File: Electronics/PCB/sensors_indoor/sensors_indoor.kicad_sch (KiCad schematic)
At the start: 10 parts, among them J1 B5B-ZR, U1 SHT45-AD1F, U2 LPS22DF, U3 SCD41-D-R2, U4 TSOP38436, U5 STM32WBA5MMG, U6 SGP41, U7 SPS30

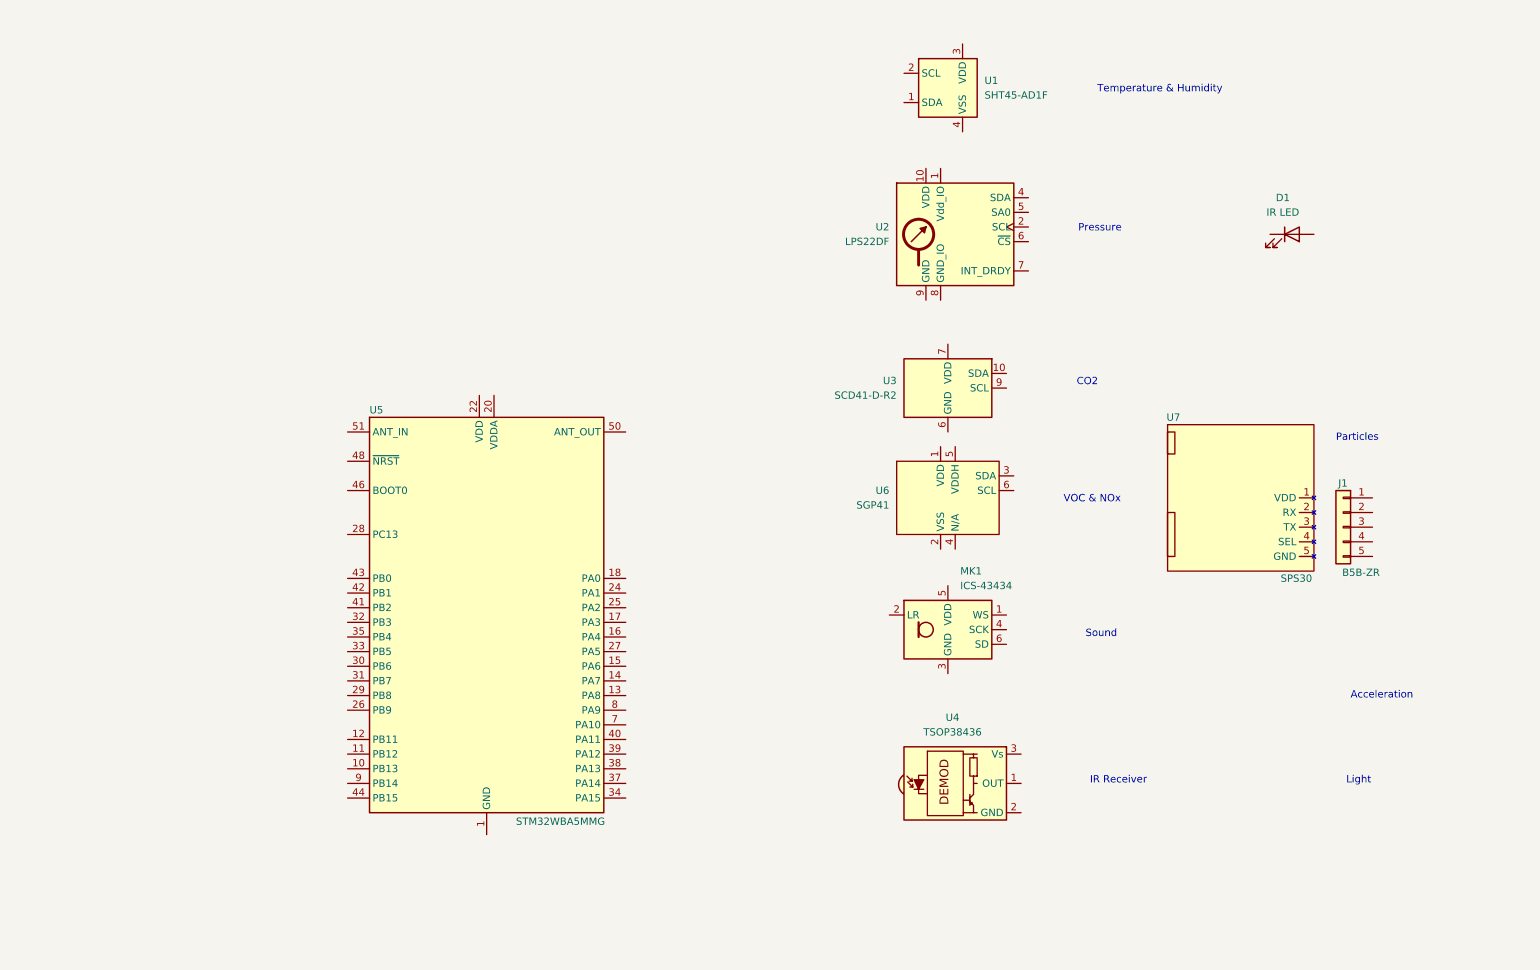
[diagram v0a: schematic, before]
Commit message: Arranged sensors on PCB, added MRAM and USB-C socket
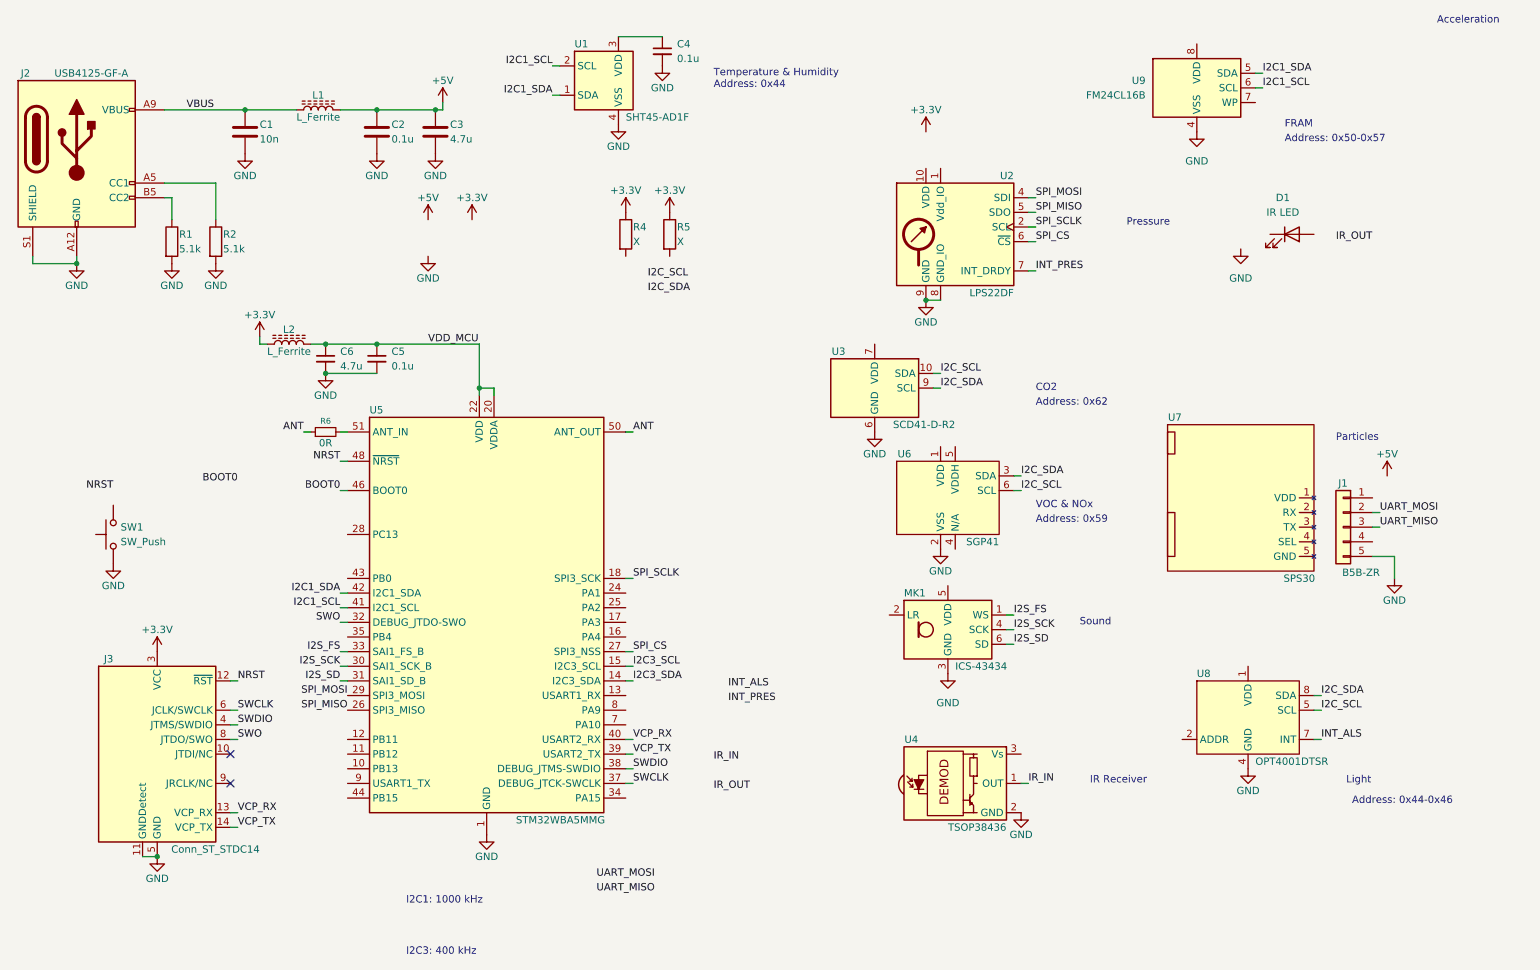
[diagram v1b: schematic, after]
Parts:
- added C1: 10n, symbol Device:C
- added C2: 0.1u, symbol Device:C
- added C3: 4.7u, symbol Device:C
- added C4, C5: 0.1u, symbol Device:C_Small
- added C6: 4.7u, symbol Device:C_Small
- added J2: USB4125-GF-A, Connector_USB:USB_C_Receptacle_GCT_USB4125-xx-x-0190_6P_TopMnt_Horizontal, symbol Connector:USB_C_Receptacle_PowerOnly_6P
- added J3: Conn_ST_STDC14, Connector_PinHeader_1.27mm:PinHeader_2x07_P1.27mm_Vertical, symbol Connector:Conn_ST_STDC14
- added L1, L2: L_Ferrite, symbol Device:L_Ferrite
- added R1, R2: 5.1k, symbol Device:R
- added R4, R5: X, symbol Device:R
- added R6: 0R, Resistor_SMD:R_0402_1005Metric, symbol Device:R_Small
- added SW1: SW_Push, symbol Switch:SW_Push
- added U8: OPT4001DTSR, DWlib:TI_SOT-5X3_OPT4001DTSR, symbol DWlib:OPT4001DTSR
- added U9: FM24CL16B, Package_SO:SOIC-8_3.9x4.9mm_P1.27mm, symbol Memory_NVRAM:FM24CL16B
- D1: footprint LED_SMD:LED_0603_1608Metric -> LED_THT:LED_D5.0mm_Clear
- U5: MPN (none) -> STM32WBA5MMGH6TR
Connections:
- net GND: now also J1.5 (Pin_5), MK1.3 (GND), U1.4 (VSS), U2.3 (GND), U2.8 (GND_IO), U2.9 (GND), U3.20 (GND), U3.21 (GND), U3.6 (GND), U4.2 (GND), U6.2 (VSS), C1.2, C2.2, C3.2, C4.2, C5.2, C6.2, J2.A12 (GND), J2.B12 (GND), J2.S1 (SHIELD), J3.11 (GNDDetect), J3.5 (GND), J3.7 (GND), R1.2, R2.2, SW1.1, U8.4 (GND), U9.4 (VSS)
- net I2C_SCL: now reaches U3.10 (SDA)
- net I2C_SCL: now also U6.6 (SCL), U8.5 (SCL)
- net I2C_SDA: now reaches U3.9 (SCL)
- net I2C_SDA: now also U6.3 (SDA), U8.8 (SDA)
- net I2S_FS: now reaches MK1.1 (WS)
- net I2S_FS: now also U5.33 (PB5)
- net I2S_SCK: now reaches MK1.4 (SCK)
- net I2S_SCK: now also U5.30 (PB6)
- net I2S_SD: now reaches MK1.6 (SD)
- net I2S_SD: now also U5.31 (PB7)
- net SPI_SCLK: now reaches U2.2 (SCL)
- net SPI_SCLK: now also U5.18 (PA0)
- net SPI_MOSI: now reaches U2.4 (SDA)
- net SPI_MOSI: now also U5.29 (PB8)
- net SPI_MISO: now reaches U2.5 (SA0)
- net SPI_MISO: now also U5.26 (PB9)
- net SPI_CS: now reaches U2.6 (~{CS})
- net SPI_CS: now also U5.27 (PA5)
- net INT_PRES: now reaches U2.7 (INT_DRDY)
- net I2C1_SDA: now reaches U1.1 (SDA)
- net I2C1_SDA: now also U5.42 (PB1), U9.5 (SDA)
- net I2C1_SCL: now reaches U1.2 (SCL)
- net I2C1_SCL: now also U5.41 (PB2), U9.6 (SCL)
- net at U1.3 (VDD): now also C4.1
- net IR_IN: now reaches U4.1 (OUT)
- net UART_MOSI: now reaches J1.2 (Pin_2)
- net UART_MISO: now reaches J1.3 (Pin_3)
- net I2C3_SDA: now reaches U5.14 (PA7)
- net I2C3_SCL: now reaches U5.15 (PA6)
- net VDD_MCU: now reaches U5.20 (VDDA)
- net VDD_MCU: now also U5.22 (VDD), C5.1, C6.1, L2.2
- net SWO: now reaches U5.32 (PB3)
- net SWO: now also J3.8 (JTDO/SWO)
- net SWCLK: now reaches U5.37 (PA14)
- net SWCLK: now also J3.6 (JCLK/SWCLK)
- net SWDIO: now reaches U5.38 (PA13)
- net SWDIO: now also J3.4 (JTMS/SWDIO)
- net VCP_TX: now reaches U5.39 (PA12)
- net VCP_TX: now also J3.14 (VCP_TX)
- net VCP_RX: now reaches U5.40 (PA11)
- net VCP_RX: now also J3.13 (VCP_RX)
- net BOOT0: now reaches U5.46 (BOOT0)
- net NRST: now reaches U5.48 (~{NRST})
- net NRST: now also J3.12 (~{RST})
- net ANT: now reaches U5.50 (ANT_OUT)
- net ANT: now also R6.1
- net at U5.51 (ANT_IN): now also R6.2
- new net: J2.B5 (CC2), R1.1
- new net: J2.A5 (CC1), R2.1
- new net +3.3V: J3.3 (VCC), L2.1, R4.1, R5.1
- new net +5V: C2.1, C3.1, L1.2
- new net INT_ALS: U8.7 (INT)
- new net VBUS: C1.1, J2.A9 (VBUS), J2.B9 (VBUS), L1.1
- no-connect marks 0 -> 2
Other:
- note added: "Address: 0x44"
- note added: "Address: 0x44-0x46"
- note added: "Address: 0x50-0x57"
- note added: "Address: 0x59"
- note added: "Address: 0x62"
- note added: "FRAM"
- note added: "I2C1: 1000 kHz"
- note added: "I2C3: 400 kHz"
- moved on the sheet: U1, U3

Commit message: Split schematic into 3 for clarity
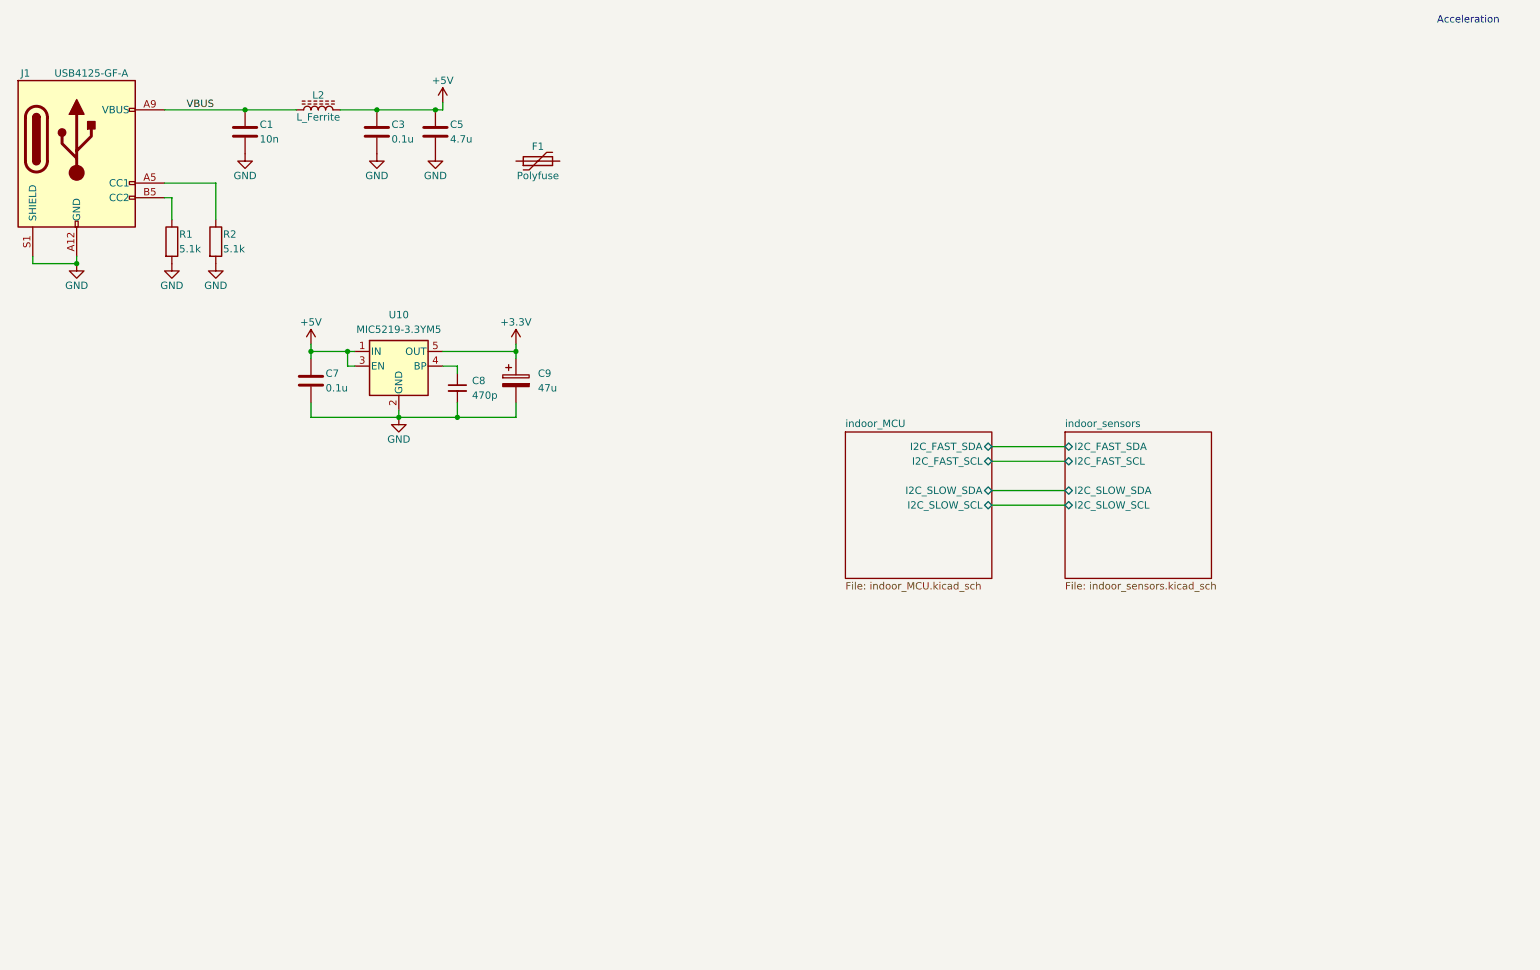
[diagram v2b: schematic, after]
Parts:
- removed C4, C5: 0.1u, symbol Device:C_Small
- removed C6: 4.7u, symbol Device:C_Small
- removed D1: IR LED, LED_THT:LED_D5.0mm_Clear, symbol Device:LED
- removed J1: B5B-ZR, Connector_JST:JST_ZH_B5B-ZR_1x05_P1.50mm_Vertical, symbol Connector_Generic:Conn_01x05
- removed J3: Conn_ST_STDC14, Connector_PinHeader_1.27mm:PinHeader_2x07_P1.27mm_Vertical, symbol Connector:Conn_ST_STDC14
- removed L2: L_Ferrite, symbol Device:L_Ferrite
- removed MK1: ICS-43434, Sensor_Audio:InvenSense_ICS-43434-6_3.5x2.65mm, symbol Sensor_Audio:ICS-43434
- removed R4, R5: X, symbol Device:R
- removed R6: 0R, Resistor_SMD:R_0402_1005Metric, symbol Device:R_Small
- removed SW1: SW_Push, symbol Switch:SW_Push
- removed U1: SHT45-AD1F, Sensor_Humidity:Sensirion_DFN-4_1.5x1.5mm_P0.8mm_SHT4x_NoCentralPad, symbol Sensor_Humidity:SHT4x
- removed U2: LPS22DF, Package_LGA:ST_HLGA-10_2x2mm_P0.5mm_LayoutBorder3x2y, symbol Sensor_Pressure:LPS22DF
- removed U3: SCD41-D-R2, Sensor:Sensirion_SCD4x-1EP_10.1x10.1mm_P1.25mm_EP4.8x4.8mm, symbol Sensor_Gas:SCD41-D-R2
- removed U4: TSOP38436, OptoDevice:Vishay_MINICAST-3Pin, symbol Interface_Optical:TSOP384xx
- removed U5: STM32WBA5MMG, DWlib:STM32WBA5MMG, symbol DWlib:STM32WBA5MMG
- removed U6: SGP41, DWlib:Sensirion_DFN-6-1EP_2.44x2.44mm_P0.5mm_EP1.25x1.7mm_SGP4x, symbol DWlib:SGP41
- removed U7: SPS30, DWlib:Sensiron_SPS30, symbol DWlib:SPS30
- removed U8: OPT4001DTSR, DWlib:TI_SOT-5X3_OPT4001DTSR, symbol DWlib:OPT4001DTSR
- removed U9: FM24CL16B, Package_SO:SOIC-8_3.9x4.9mm_P1.27mm, symbol Memory_NVRAM:FM24CL16B
- added C7: 0.1u, symbol Device:C
- added C8: 470p, symbol Device:C_Small
- added C9: 47u, Capacitor_Tantalum_SMD:CP_EIA-7343-31_Kemet-D, symbol Device:C_Polarized
- added F1: Polyfuse, symbol Device:Polyfuse
- added U10: MIC5219-3.3YM5, Package_TO_SOT_SMD:SOT-23-5, symbol Regulator_Linear:MIC5219-3.3YM5
- renumbered C2 to C3, C3 to C5, J2 to J1, L1 to L2
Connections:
- net +3.3V: now also C9.1, U10.5 (OUT)
- net +5V: now also C7.1, U10.1 (IN), U10.3 (EN)
- net GND: now also C7.2, C8.2, C9.2, U10.2 (GND)
- new net: C8.1, U10.4 (BP)
- no-connect marks 2 -> 0
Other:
- added sheet indoor_MCU (indoor_MCU.kicad_sch)
- added sheet indoor_sensors (indoor_sensors.kicad_sch)
- note removed: "Address: 0x44"
- note removed: "Address: 0x44-0x46"
- note removed: "Address: 0x50-0x57"
- note removed: "Address: 0x59"
- note removed: "Address: 0x62"
- note removed: "CO2"
- note removed: "FRAM"
- note removed: "I2C1: 1000 kHz"
- note removed: "I2C3: 400 kHz"
- note removed: "IR Receiver"
- note removed: "Light"
- note removed: "Particles"
- note removed: "Pressure"
- note removed: "Sound"
- note removed: "Temperature & Humidity"
- note removed: "VOC & NOx"

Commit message: Added mounting holes and power supply
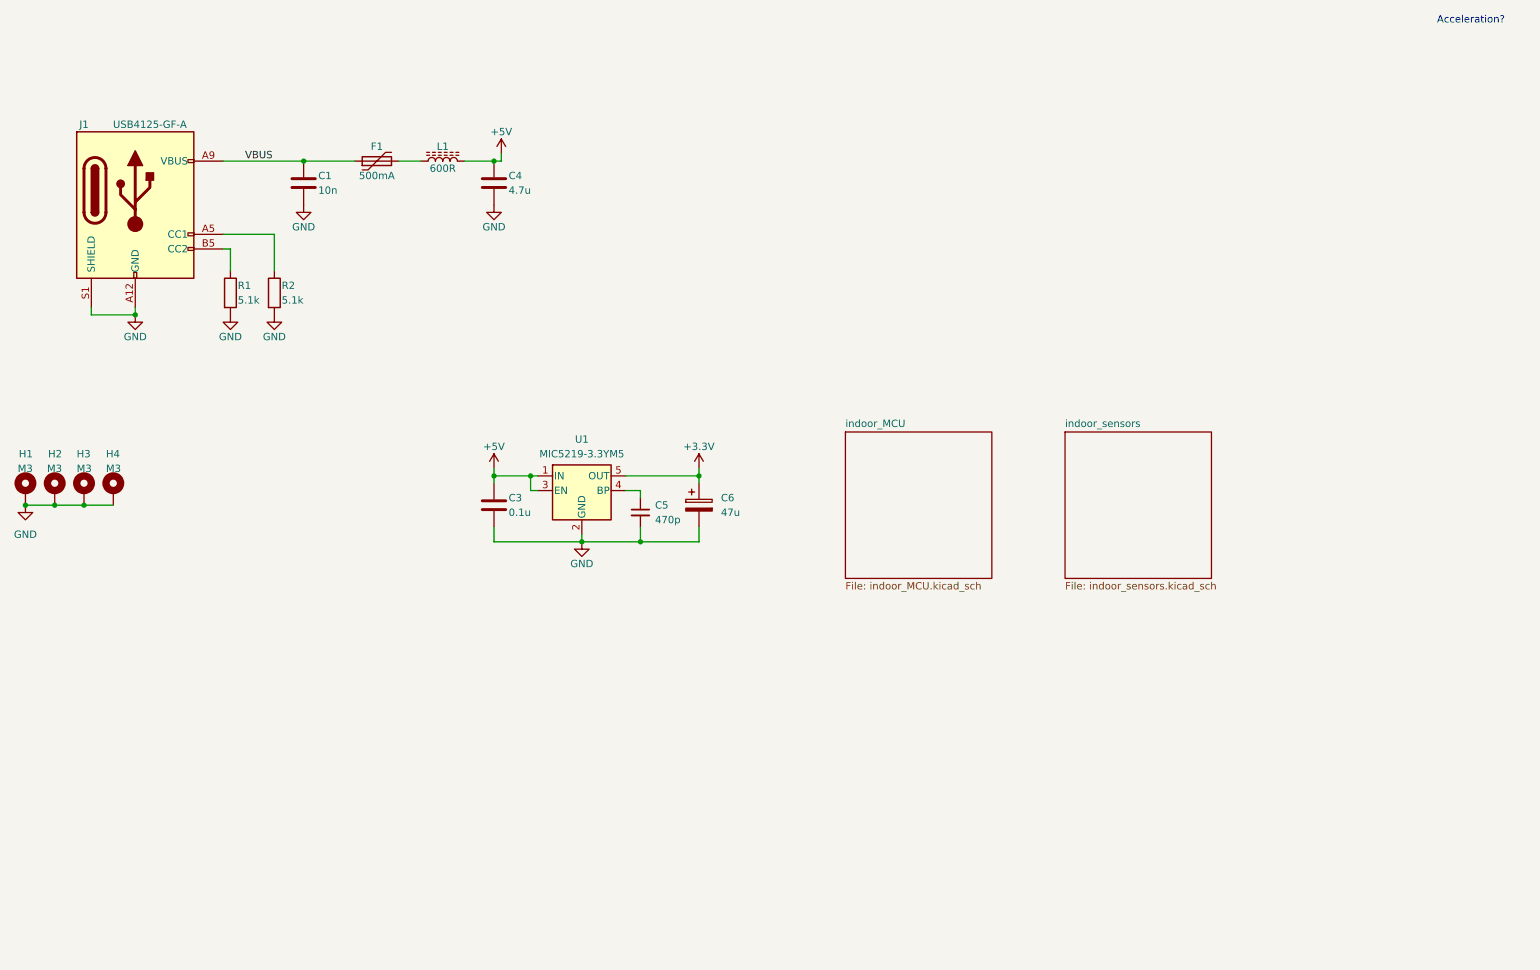
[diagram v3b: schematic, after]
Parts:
- removed C3: 0.1u, symbol Device:C
- added H1, H2, H3, H4: M3, MountingHole:MountingHole_3.2mm_M3_Pad, symbol Mechanical:MountingHole_Pad
- C3: renamed from C7; footprint (none) -> Capacitor_SMD:C_0402_1005Metric
- C4: renamed from C5; footprint (none) -> Capacitor_SMD:C_0805_2012Metric
- F1: value Polyfuse -> 500mA; footprint (none) -> Fuse:Fuse_0805_2012Metric
- L1: renamed from L2; value L_Ferrite -> 600R; footprint (none) -> Inductor_SMD:L_0805_2012Metric; MPN (none) -> HZ0805E601R-10; Mouser PN (none) -> 875-HZ0805E601R-10
- R1, R2: footprint (none) -> Resistor_SMD:R_0603_1608Metric
- renumbered C8 to C5, C9 to C6, U10 to U1
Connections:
- net GND: now also H1.1, H2.1, H3.1, H4.1
- net VBUS: now also F1.1; no longer L1.1
- net at F1.2: now also L1.1
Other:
- sheet indoor_MCU ports: added none; removed I2C_FAST_SCL, I2C_FAST_SDA, I2C_SLOW_SCL, I2C_SLOW_SDA
- sheet indoor_sensors ports: added none; removed I2C_FAST_SCL, I2C_FAST_SDA, I2C_SLOW_SCL, I2C_SLOW_SDA
- note added: "Acceleration?"
- note removed: "Acceleration"
- moved on the sheet: C1, C3, C4, C5, C6, F1, J1, L1, R1, R2, U1
